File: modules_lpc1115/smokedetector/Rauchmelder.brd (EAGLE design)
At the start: 38 x 65 mm, 75 parts, among them IC1 BD9G101, IC2 LPC1115, Q1 BC856, Q3 BCP52, Q4 ASFL, T1 BC847C, T2 BC817

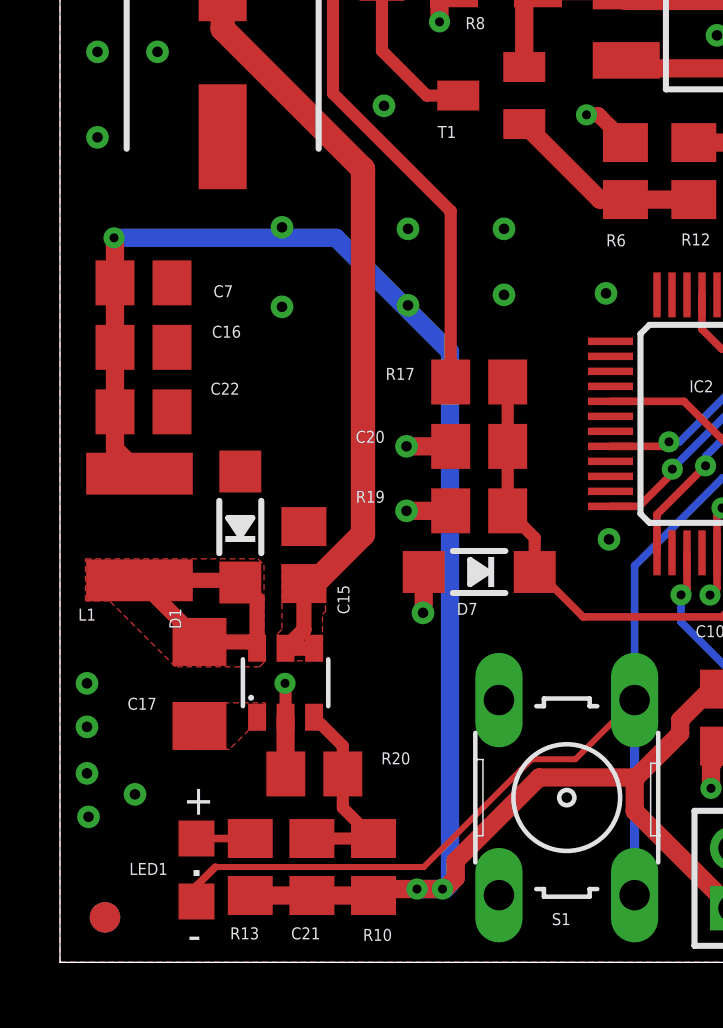
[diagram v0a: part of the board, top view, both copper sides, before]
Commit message: [RM] - changed values to standard values
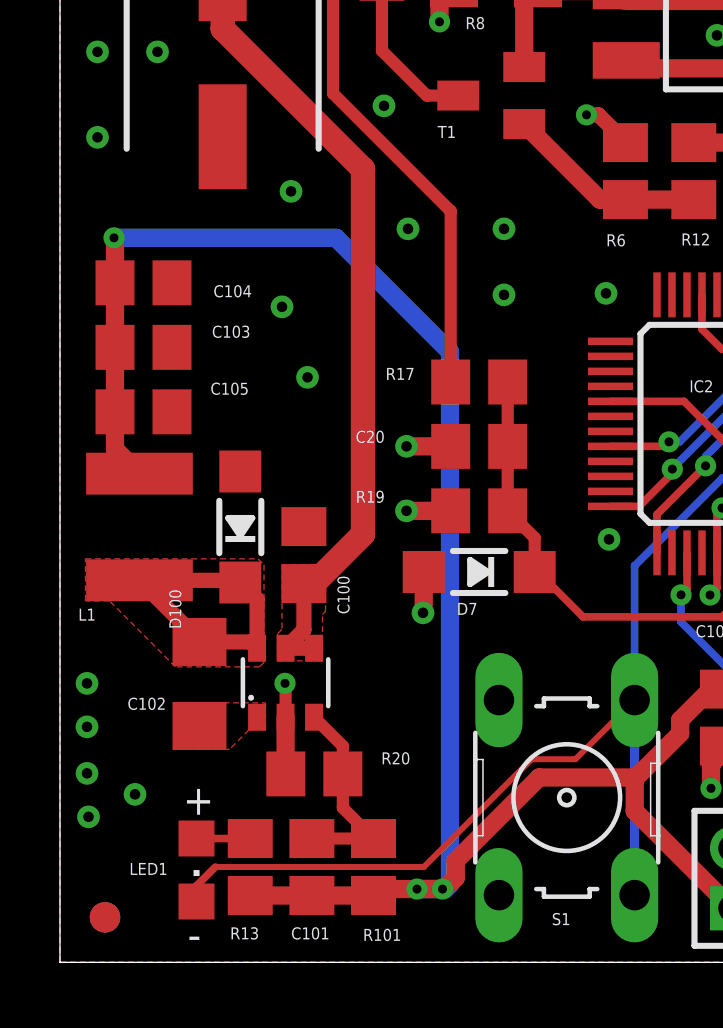
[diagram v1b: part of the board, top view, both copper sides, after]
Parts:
- C103, C105: value 47uF/10V -> 47uF 10V
- C11, C8: value 10n -> 10nF
- L1: value 6.8µH -> 6.8uH
- renumbered C15 to C100, C16 to C103, C17 to C102, C21 to C101, C22 to C105, C7 to C104, D1 to D100, R10 to R101
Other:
- board text added: "Selfbus RM-ARM v3.8.3 beta1"
- board text removed: "Selfbus RM-ARM v3.8.3"
